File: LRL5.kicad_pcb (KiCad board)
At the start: 2 copper layers, 96.2 x 50 mm, 31 parts, among them J1 POWER, J2 On/Off, J5 OUT, J6 MODE, Q1 BC549, U1 BA033CC0T, U2 NHD-C0220BIZ

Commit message: Some fixes 2
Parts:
- added J7: DEBUG, Connector_PinHeader_2.54mm:PinHeader_1x03_P2.54mm_Vertical_SMD_Pin1Left, F.Cu at (194.6, 53.6)
- moved R5 4.09 mm to (188.4, 62.2), turned to 90 degrees
- moved R2 3.17 mm to (197.8, 67.0)
- moved R1 2.02 mm to (203.6, 64.2), turned to -90 degrees
- moved C1 1.40 mm to (205.4, 69.4)
- moved TP2 0.51 mm to (185.0, 76.4)
- moved TP1 0.18 mm to (191.4, 76.4)
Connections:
- J3 pad 14: unconnected-(J3-Pin_14-Pad14) -> UART1_RX
- J3 pad 15: unconnected-(J3-Pin_15-Pad15) -> UART1_TX
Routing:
- net UART1_TX: track 0.00 -> 27.4 mm, vias 0 -> 2
- net UART1_RX: track 0.00 -> 25.0 mm, vias 0 -> 2
- net GND: track 44.1 -> 60.8 mm
- net Net-(D2-K): track 94.4 -> 91.2 mm
- net +BATT: track 53.4 -> 56.1 mm, vias 0 -> 1
- net VBAT: track 58.9 -> 61.4 mm
- net MODE_SW1: track 77.1 -> 77.7 mm
- net MODE_A: track 71.9 -> 72.4 mm
- net +3.3V: track 100.3 -> 100.8 mm
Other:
- board text added: "DEBUG"
- board text added: "OUT"
- board text added: "On/Off"
- board text added: "RX"
- board text added: "TX"

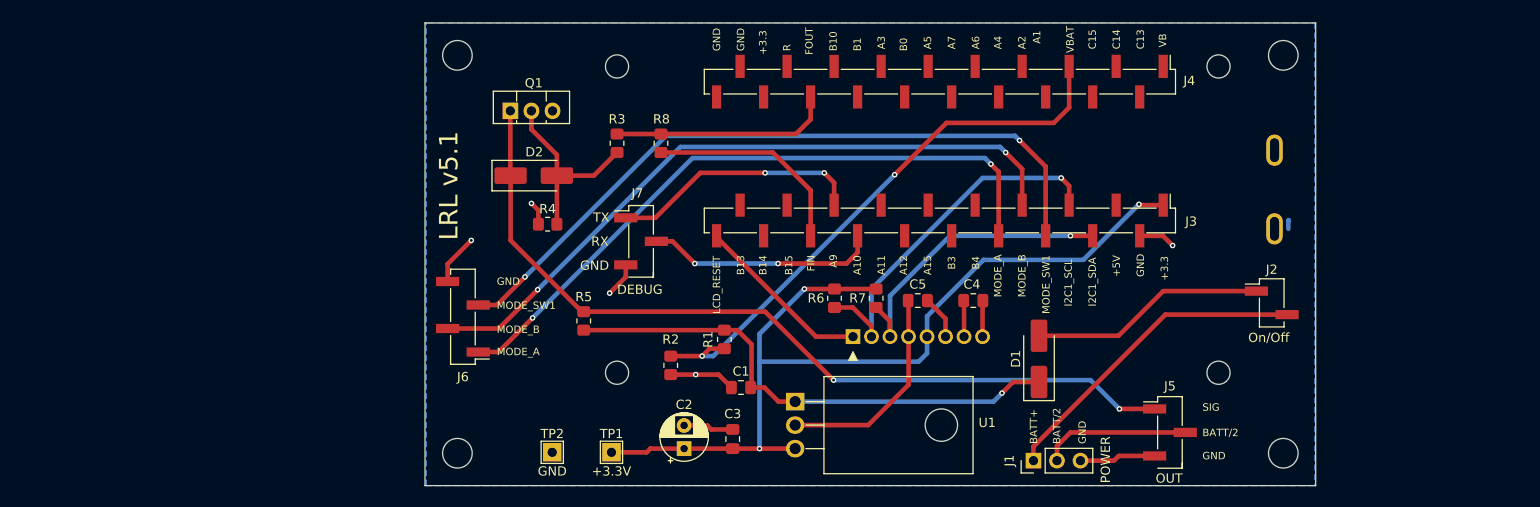
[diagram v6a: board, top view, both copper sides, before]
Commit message: Add DEBUG connector
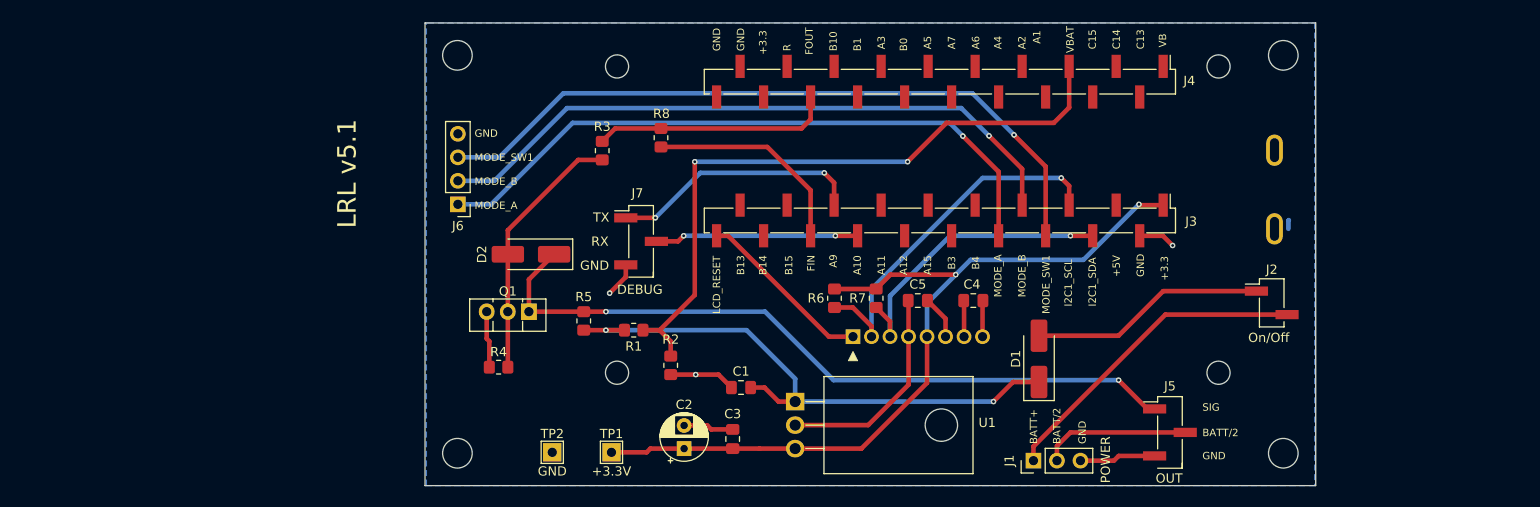
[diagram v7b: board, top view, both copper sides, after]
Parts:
- J6: footprint Connector_PinHeader_2.54mm:PinHeader_1x04_P2.54mm_Vertical_SMD_Pin1Left -> Connector_PinHeader_2.54mm:PinHeader_1x04_P2.54mm_Vertical
- moved Q1 21.8 mm to (182.5, 61.2), turned to 180 degrees
- moved R4 16.3 mm to (179.2, 67.2)
- moved J6 12.2 mm to (174.8, 49.6)
- moved R1 9.85 mm to (193.8, 63.2), turned to 0 degrees
- moved D2 8.51 mm to (182.7, 55.0), turned to 180 degrees
- moved R3 1.79 mm to (190.4, 43.8)
- moved R8 0.60 mm to (196.8, 42.4)
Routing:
- net Net-(D2-K): track 91.2 -> 79.3 mm
- net VBAT: track 61.4 -> 72.2 mm
- net +3.3V: track 100.8 -> 90.2 mm, vias 3 -> 2
- net Net-(D2-A): track 20.9 -> 28.0 mm
- net +BATT: track 56.1 -> 62.3 mm, vias 1 -> 2
- net MODE_B: track 75.3 -> 70.9 mm, vias 2 -> 1
- net UART1_RX: track 25.0 -> 22.0 mm
- net GND: track 60.8 -> 58.8 mm, vias 5 -> 3
- net FOUT: track 24.0 -> 25.9 mm
- net MODE_A: track 72.4 -> 71.2 mm, vias 2 -> 1
- net MODE_SW1: track 77.7 -> 77.1 mm, vias 2 -> 1

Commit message: Fix version text
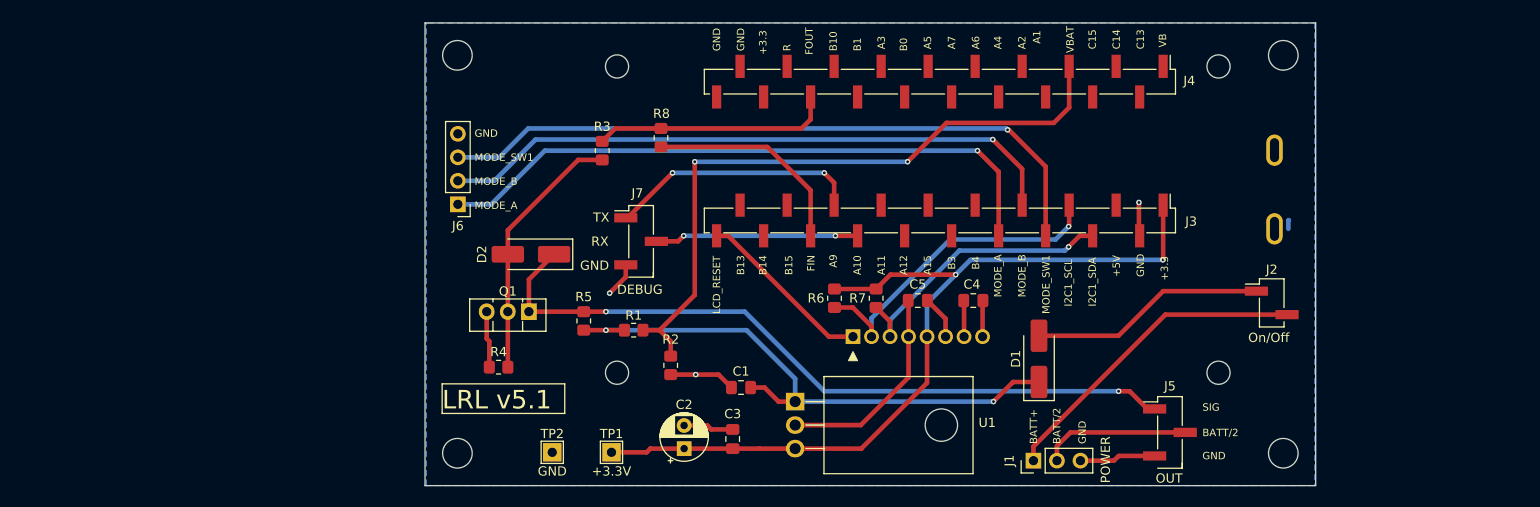
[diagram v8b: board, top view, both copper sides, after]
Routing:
- net I2C1_SCL: track 39.9 -> 35.7 mm
- net +3.3V: track 90.2 -> 93.6 mm
- net MODE_SW1: track 77.1 -> 74.0 mm
- net MODE_B: track 70.9 -> 68.1 mm
- net MODE_A: track 71.2 -> 68.7 mm
- net I2C1_SDA: track 32.8 -> 31.2 mm
- net GND: track 58.8 -> 58.0 mm
